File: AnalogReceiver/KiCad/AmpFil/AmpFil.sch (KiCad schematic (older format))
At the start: 38 parts, among them P1 Header2x1, P2 Header2x1, P3 Header2x1, P4 Header2x1, U1 LT1677, U2 LT1677, U3 LT1677, U4 LT1677

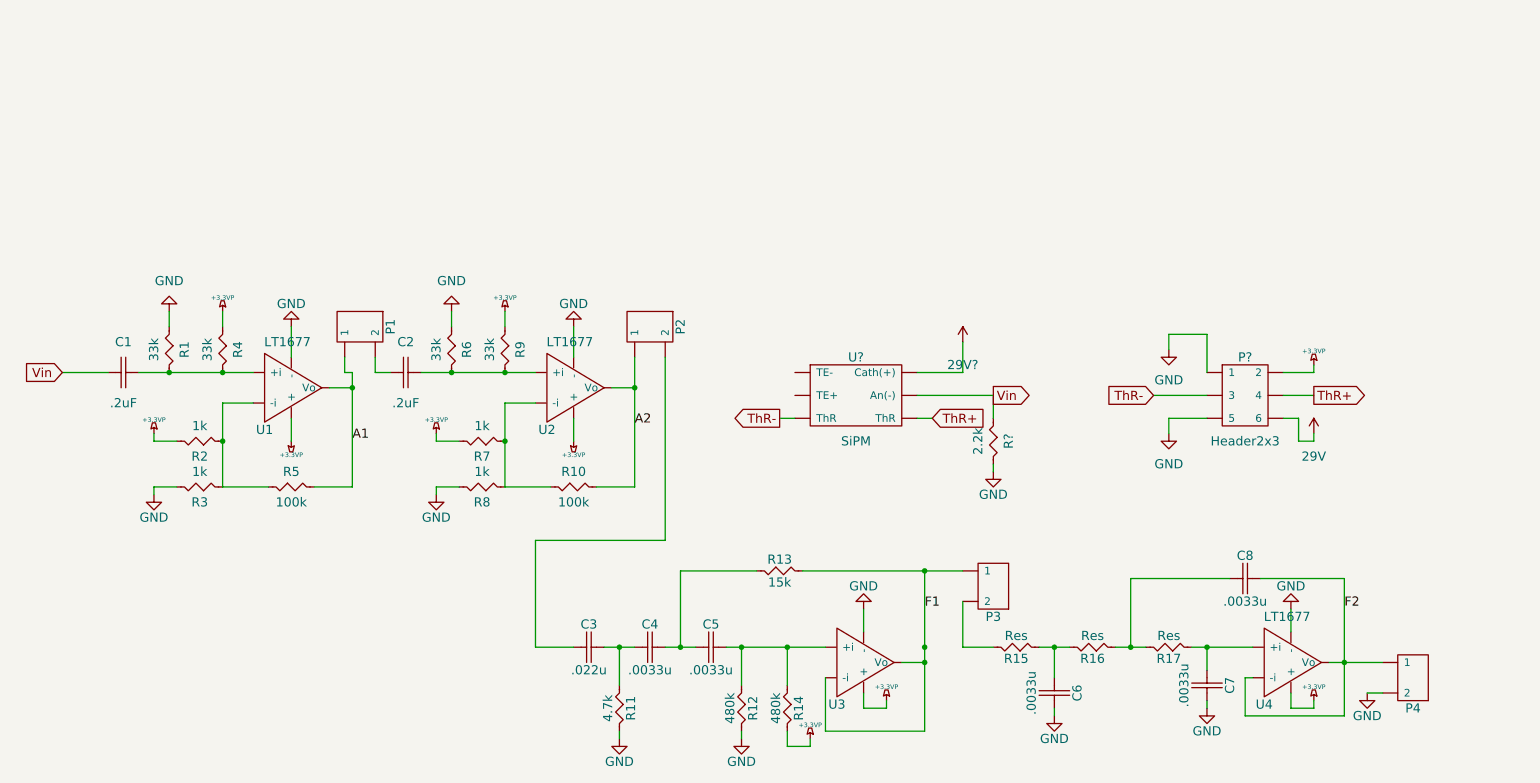
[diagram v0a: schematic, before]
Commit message: New Work on PCB
I did a lot of work and development on the PCB for the
amplifier/filter. There should be a bunch of new files and
modifications.
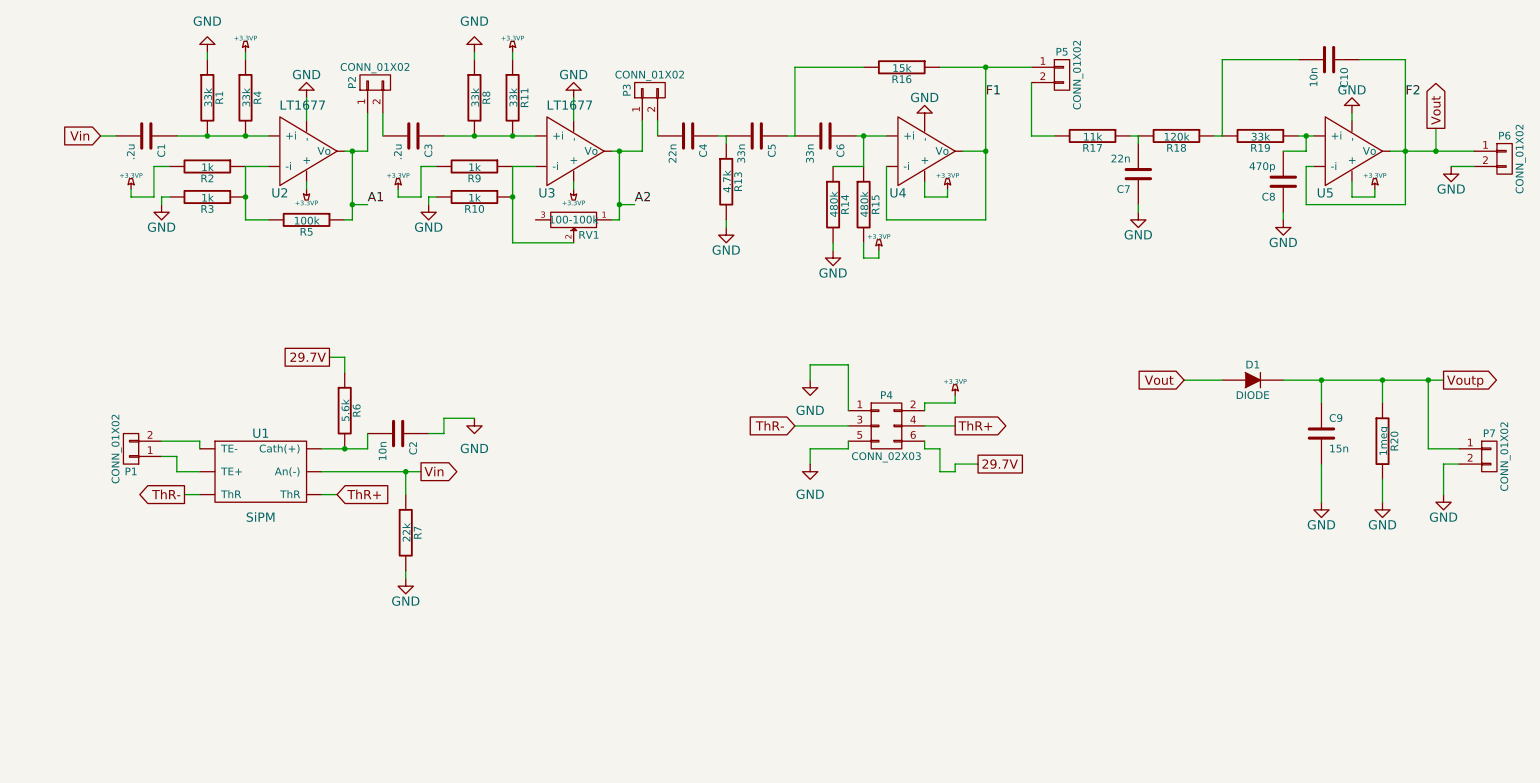
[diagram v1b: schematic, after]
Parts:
- removed 29V, 29V?: +36V, symbol +36V
- removed C1, C2: .2uF, symbol Cap
- removed C3: .022u, symbol Cap
- removed C4, C5, C6, C7, C8: .0033u, symbol Cap
- removed P1, P2, P3, P4: Header2x1, symbol Header2x1
- removed P?: Header2x3, symbol Header2x3
- removed R1, R4, R6, R9: 33k, symbol Res
- removed R10, R5: 100k, symbol Res
- removed R11: 4.7k, symbol Res
- removed R12, R14: 480k, symbol Res
- removed R13: 15k, symbol Res
- removed R15, R16, R17: Res, symbol Res
- removed R2, R3, R7, R8: 1k, symbol Res
- removed R?: 2.2k, symbol Res
- removed U2: LT1677, symbol LT1677
- added C1, C3: .2u, Capacitors_ThroughHole:Capacitor13x4RM10, symbol C
- added C10, C2: 10n, Capacitors_ThroughHole:Capacitor13x4RM10, symbol C
- added C4, C7: 22n, Capacitors_ThroughHole:Capacitor13x4RM10, symbol C
- added C5, C6: 33n, Capacitors_ThroughHole:Capacitor13x4RM10, symbol C
- added C8: 470p, Capacitors_ThroughHole:Capacitor13x4RM10, symbol C
- added C9: 15n, Capacitors_ThroughHole:Capacitor13x4RM10, symbol C
- added D1: DIODE, Diodes_ThroughHole:Diode_DO-35_SOD27_Horizontal_RM10, symbol DIODE
- added P1, P2, P3, P5: CONN_01X02, Pin_Headers:Pin_Header_Angled_2x01, symbol CONN_01X02
- added P4: CONN_02X03, Pin_Headers:Pin_Header_Angled_2x03, symbol CONN_02X03
- added P6, P7: CONN_01X02, Pin_Headers:Pin_Header_Angled_1x02, symbol CONN_01X02
- added R1, R11, R19, R4, R8: 33k, Resistors_ThroughHole:Resistor_Horizontal_RM10mm, symbol R
- added R10, R2, R3, R9: 1k, Resistors_ThroughHole:Resistor_Horizontal_RM10mm, symbol R
- added R13: 4.7k, Resistors_ThroughHole:Resistor_Horizontal_RM10mm, symbol R
- added R14, R15: 480k, Resistors_ThroughHole:Resistor_Horizontal_RM10mm, symbol R
- added R16: 15k, Resistors_ThroughHole:Resistor_Horizontal_RM10mm, symbol R
- added R17: 11k, Resistors_ThroughHole:Resistor_Horizontal_RM10mm, symbol R
- added R18: 120k, Resistors_ThroughHole:Resistor_Horizontal_RM10mm, symbol R
- added R20: 1meg, Resistors_ThroughHole:Resistor_Horizontal_RM10mm, symbol R
- added R5: 100k, Resistors_ThroughHole:Resistor_Horizontal_RM10mm, symbol R
- added R6: 5.6k, Resistors_ThroughHole:Resistor_Horizontal_RM10mm, symbol R
- added R7: 22k, Resistors_ThroughHole:Resistor_Horizontal_RM10mm, symbol R
- added RV1: 100-100k, Potentiometers:Potentiometer_Trimmer-Suntan-TSR-3386C, symbol POT
- added U3: LT1677, Sockets_DIP:DIP-8__300, symbol LT1677
- U1: renamed from U?; footprint (none) -> mylib:SiPM
- U2: renamed from U1; footprint (none) -> Sockets_DIP:DIP-8__300
- U4: renamed from U3; footprint (none) -> Sockets_DIP:DIP-8__300
- U5: renamed from U4; footprint (none) -> Sockets_DIP:DIP-8__300
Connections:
- net +3.3VP: now also P4.2 (P2), R11.1, R15.2, R2.2, R4.1, R9.2, U3.7 (+)
- net A1: now also P2.1 (P1), R5.1
- net A2: now also P3.1 (P1), RV1.1, U3.6 (Vo)
- net F1: now also P5.1 (P1), R16.1
- net GND: now also C2.1, C7.1, C8.1, C9.2, P4.1 (P1), P4.5 (P5), P6.2 (P2), P7.2 (P2), R1.1, R10.2, R13.2, R14.2, R20.2, R3.2, R7.2, R8.1, U3.4 (-)
- net ThR+: now also P4.4 (P4)
- net ThR-: now also P4.3 (P3)
- net Vin: now also C1.2, R7.1
- net at U2.2 (-i): now also R2.1, R3.1, R5.2
- net at U2.3 (+i): now also C1.1, R1.2, R4.2
- net at U4.3 (+i): now also C6.1, R14.1, R15.1
- net at U5.3 (+i): now also C8.2, R19.1
- net at U1.1 (TE-): now also P1.2 (P2)
- net at U1.2 (TE+): now also P1.1 (P1)
- net +36V: no longer names the net of U1.6 (Cath(+))
- net +36V: now also C2.2, R6.2
- net F2 renamed Vout
- net Vout: now also C10.1, D1.1 (A), P6.1 (P1)
- new net: C4.2, P3.2 (P2)
- new net: C3.2, P2.2 (P2)
- new net: P5.2 (P2), R17.2
- new net: R10.1, R9.1, RV1.2, U3.2 (-i)
- new net: C3.1, R11.2, R8.2, U3.3 (+i)
- new net: C4.1, C5.2, R13.1
- new net: C5.1, C6.2, R16.2
- new net: C7.2, R17.1, R18.2
- new net: C10.2, R18.1, R19.2
- new net 29.7V: P4.6 (P6), R6.1
- new net Voutp: C9.1, D1.2 (K), P7.1 (P1), R20.1
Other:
- moved on the sheet: U1, U2, U4, U5
